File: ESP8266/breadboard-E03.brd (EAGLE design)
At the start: 30.5 x 21.6 mm, 12 parts, among them CON1 USBMICRO-NO_CENTER

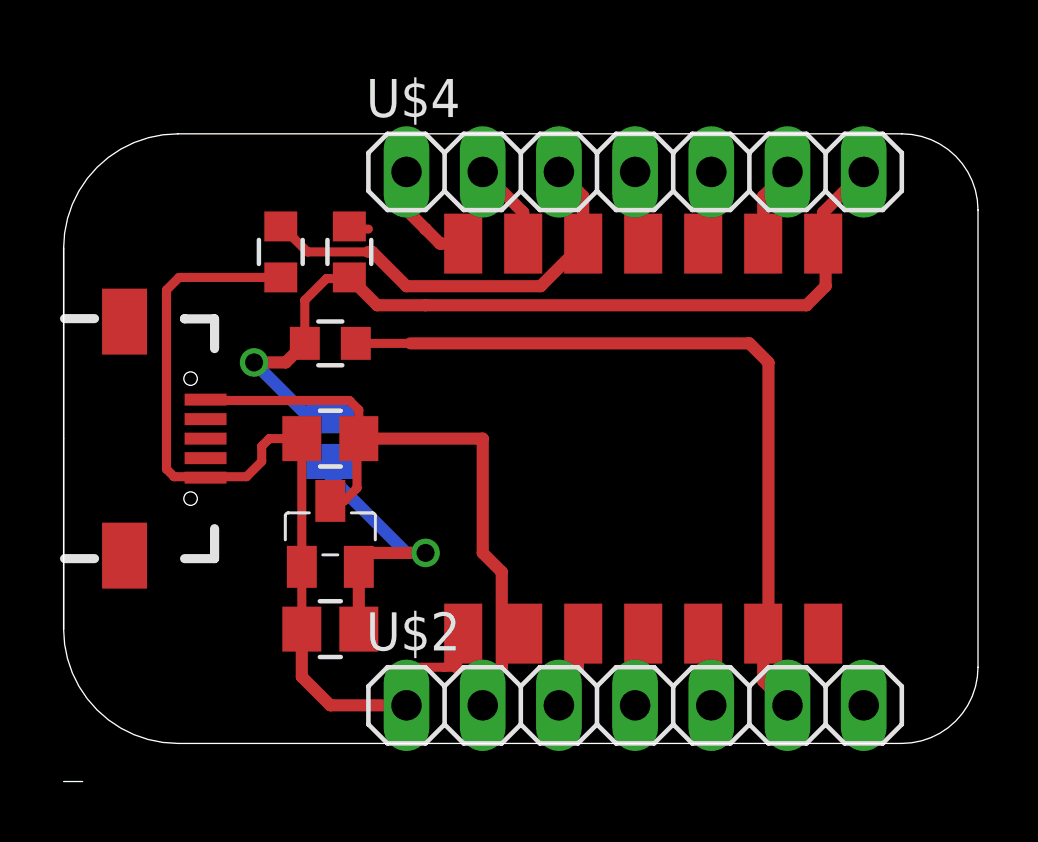
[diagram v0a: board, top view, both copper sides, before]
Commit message: switch to different vreg
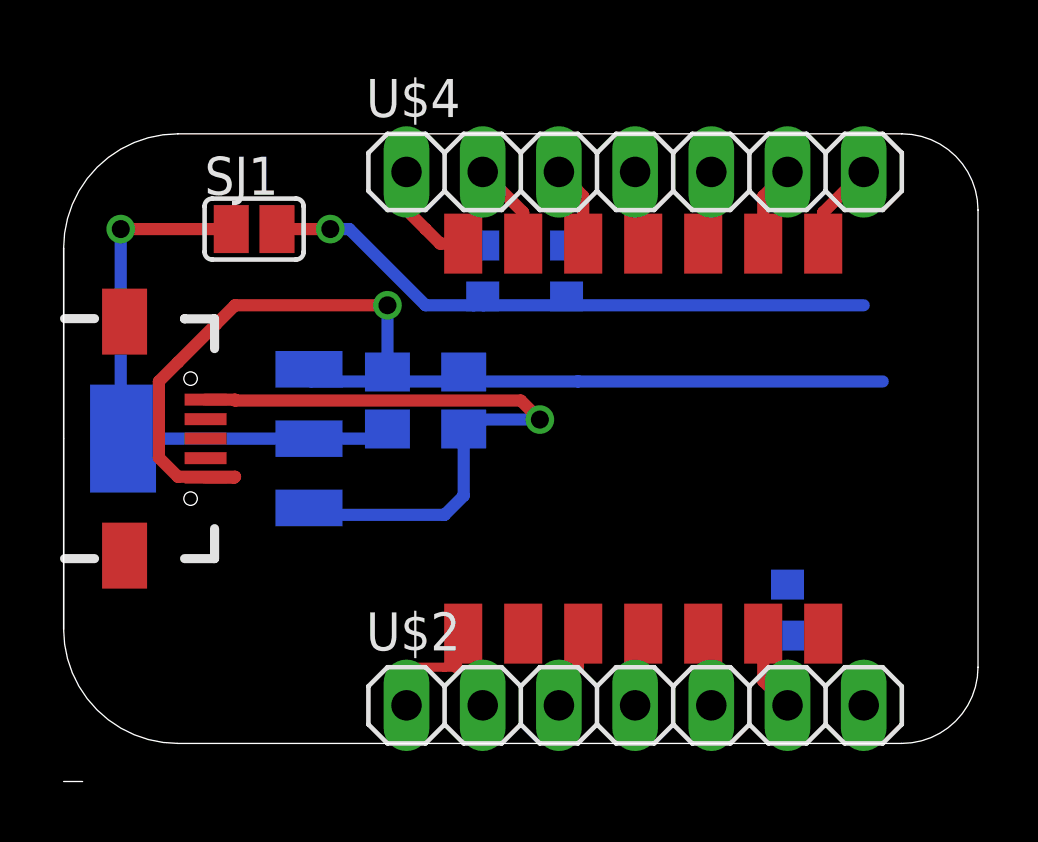
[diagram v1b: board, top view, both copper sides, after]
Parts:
- removed U1: (no value), p.peter-regulators:SOT23
- added IC1: (no value), p.peter-regulators:SOT223
- moved R3 17.6 mm to (23.5, 5.71), flipped to the bottom, turned to 90 degrees
- moved U$3 10.8 mm to (7.62, 22.2)
- moved R1 9.55 mm to (16.1, 17.0), flipped to the bottom
- moved C2 7.85 mm to (10.2, 12.7), flipped to the bottom, turned to 90 degrees
- moved SJ1 7.43 mm to (5.71, 18.4), flipped to the top, turned to 0 degrees
- moved C1 4.62 mm to (12.7, 12.7), flipped to the bottom, turned to 90 degrees
- moved R2 4.49 mm to (13.3, 17.0), flipped to the bottom
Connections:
- net +5V: now also IC1.3; no longer U1.P$3
- net GND: now also IC1.1; no longer U1.P$1
- net N$1: now also IC1.2, IC1.4; no longer U1.P$2
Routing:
- net RESET: track 26.1 -> 2.73 mm
- net IO15: track 14.2 -> 2.73 mm
- net N$1: track 9.31 -> 19.8 mm
- net GND: track 32.3 -> 41.8 mm, vias 0 -> 1
- net +3V3: track 29.6 -> 24.0 mm
- net IO02: track 3.62 -> 2.95 mm
- net +5V: track 22.5 -> 21.8 mm, vias 0 -> 1
